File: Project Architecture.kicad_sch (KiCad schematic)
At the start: 0 parts

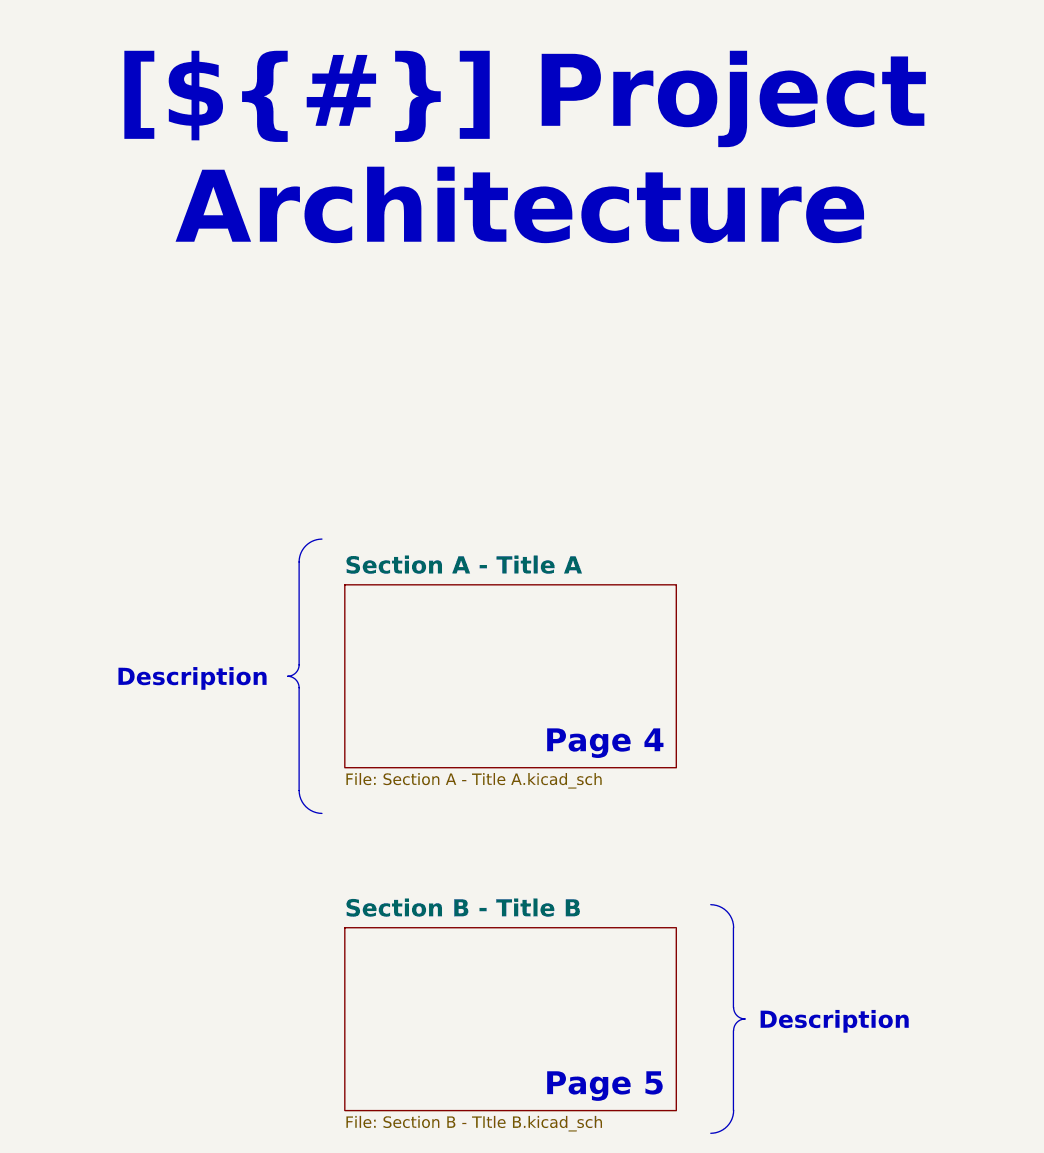
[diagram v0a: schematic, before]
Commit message: routed signals
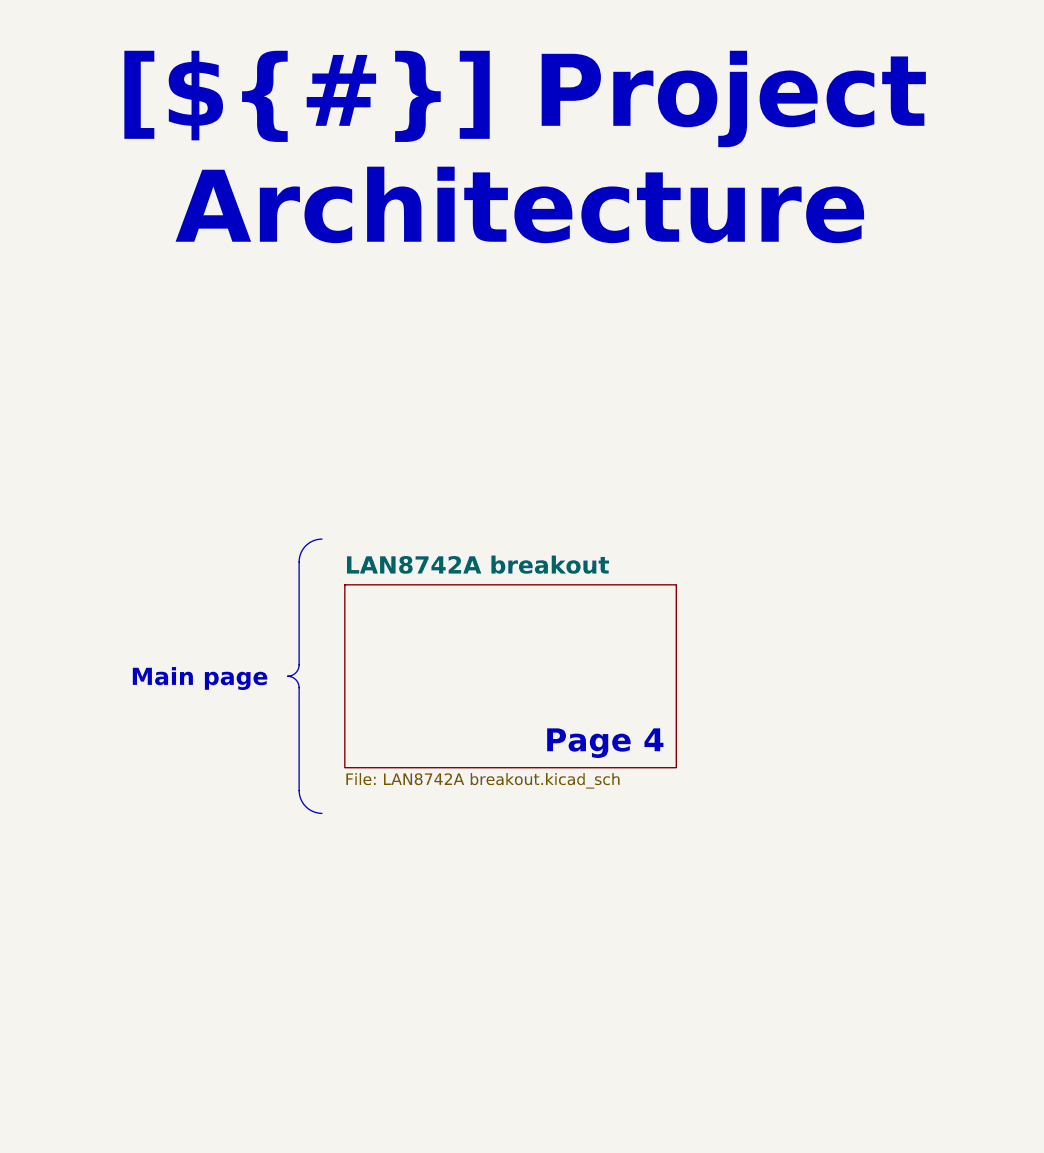
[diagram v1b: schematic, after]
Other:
- sheet Section A - Title A renamed LAN8742A breakout
- removed sheet Section B - Title B
- sheet LAN8742A breakout: file Section A - Title A.kicad_sch -> LAN8742A breakout.kicad_sch
- note removed: "Page 5"
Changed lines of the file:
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@@
-	(polyline
-		(pts
-			(xy 233.68 125.73) (xy 233.68 134.62)
-		)
-		(stroke
-			(width 0)
-			(type default)
-		)
-	)
 	(polyline
 		(pts
 			(xy 185.42 85.09) (xy 185.42 73.66)
-		)
-		(stroke
-			(width 0)
-			(type default)
-		)
-	)
-	(polyline
-		(pts
-			(xy 233.68 114.3) (xy 233.68 123.19)
 		)
 		(stroke
@@
 		(mid 185.0451 85.9851)
 		(end 184.15 86.36)
-		(stroke
-			(width 0)
-			(type default)
-		)
-		(fill
-			(type none)
-		)
-	)
-	(arc
-		(start 234.97 124.44)
-		(mid 234.0749 124.0651)
-		(end 233.7 123.17)
-		(stroke
-			(width 0)
-			(type default)
-		)
-		(fill
-			(type none)
-		)
-	)
-	(arc
-		(start 233.7 125.71)
-		(mid 234.0749 124.8149)
-		(end 234.97 124.44)
-		(stroke
-			(width 0)
-			(type default)
-		)
-		(fill
-			(type none)
-		)
-	)
-	(arc
-		(start 233.7 134.6)
-		(mid 232.9561 136.3961)
-		(end 231.16 137.14)
 		(stroke
 			(width 0)
@@
 	)
 	(arc
-		(start 231.16 111.74)
-		(mid 232.9502 112.4898)
-		(end 233.7 114.28)
-		(stroke
-			(width 0)
-			(type default)
-		)
-		(fill
-			(type none)
-		)
-	)
-	(arc
 		(start 185.42 73.66)
 		(mid 186.1639 71.8639)
@@
 		)
 	)
-	(text_box "Description"
+	(text_box "Main page"
 		(exclude_from_sim no)
-		(at 166.37 83.82 0)
-		(size 17.145 5.08)
+		(at 160.02 83.82 0)
+		(size 23.495 5.08)
 		(stroke
 			(width -0.0001)
@@
 			)
 			(justify right top)
-		)
-	)
-	(text_box "Description"
-		(exclude_from_sim no)
-		(at 234.95 121.92 0)
-		(size 26.015 5.1)
-		(stroke
-			(width -0.0001)
-			(type default)
-		)
-		(fill
-			(type none)
-		)
-		(effects
-			(font
-				(size 1.905 1.905)
-				(thickness 0.381)
-				(bold yes)
-				(color 0 0 0 1)
-			)
-			(justify left top)
 		)
 	)
@@
 		)
 	)
-	(text "Page 5"
-		(exclude_from_sim no)
-		(at 226.06 133.35 0)
-		(effects
-			(font
-				(size 2.54 2.54)
-				(bold yes)
-				(color 100 70 50 1)
-			)
-			(justify right bottom)
-			(href "#5")
-		)
-	)
 	(text "Page 4"
 		(exclude_from_sim no)
@@
 	)
 	(sheet
-		(at 190.5 114.3)
-		(size 36.83 20.32)
-		(fields_autoplaced yes)
-		(stroke
-			(width 0.1524)
-			(type solid)
-		)
-		(fill
-			(color 255 200 0 0.5020)
-		)
-		(property "Sheetname" "Section B - Title B"
-			(at 190.5 113.2709 0)
-			(effects
-				(font
-					(size 1.905 1.905)
-					(bold yes)
-				)
-				(justify left bottom)
-			)
-		)
-		(property "Sheetfile" "Section B - TItle B.kicad_sch"
-			(at 190.5 135.2046 0)
-			(effects
-				(font
-					(face "Arial")
-					(size 1.27 1.27)
-				)
-				(justify left top)
-			)
-		)
-		(instances
-			(project "LAN8742A-breakout"
-				(path "/f9e05184-c88b-4a88-ae9c-ab2bdb32be7c/c5103ceb-5325-4a84-a025-9638a412984e"
-					(page "5")
-				)
-			)
-		)
-	)
-	(sheet
 		(at 190.5 76.2)
 		(size 36.83 20.32)
@@
 			(color 128 255 128 0.5000)
 		)
-		(property "Sheetname" "Section A - Title A"
+		(property "Sheetname" "LAN8742A breakout"
 			(at 190.5 75.1709 0)
 			(effects
@@
 			)
 		)
-		(property "Sheetfile" "Section A - Title A.kicad_sch"
+		(property "Sheetfile" "LAN8742A breakout.kicad_sch"
 			(at 190.5 97.1046 0)
 			(effects
